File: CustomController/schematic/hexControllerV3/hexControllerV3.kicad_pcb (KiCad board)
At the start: 4 copper layers, 129 x 63.9 mm, 48 parts, among them IC1 ESP32-S2-MINI-1-N4R2, IC2 IP5306, J1 USB_C_Receptacle_USB2.0_16P, J2 Battery, J3 Switch1, J4 Switch2, J5 Switch3, J6 Switch4, J7 Battery, SW1 RotaryEncoder_Switch, SW2 SW_DIP_x01, SW3 SW_DIP_x01, SW4 SW_DIP_x01, SW5 SW_DIP_x01, SW6 SW_DIP_x01, U2 AMS1117-3.3

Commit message: Changed schematic/ PCB
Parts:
- moved J5 1.87 mm to (115.3, 59.8)
- moved J6 1.26 mm to (111.4, 59.8)
- moved J1 1.05 mm to (152.5, 53.8)
- moved SW6 0.60 mm to (149.4, 96.3)
- moved SW1 0.45 mm to (208.1, 74.5)
- moved SW2 0.45 mm to (100.9, 65.2)
- moved SW3 0.45 mm to (91.4, 74.7)
- moved SW4 0.45 mm to (100.9, 84.2)
- moved SW5 0.45 mm to (110.4, 74.7)
- moved VR1 0.35 mm to (125.1, 110.4)
- moved VR2 0.35 mm to (175.1, 110.4)
- moved LED5 0.32 mm to (152.6, 104.8)
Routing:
- net D-: track 15.5 -> 18.8 mm
- net GND: track 77.8 -> 81.0 mm
- net +5V USB: track 34.8 -> 37.9 mm
- net D+: track 16.4 -> 18.0 mm
- net Switch3: track 49.8 -> 50.9 mm
- net Net-(J1-CC2): track 10.4 -> 11.4 mm
- net Switch4: track 49.5 -> 50.1 mm
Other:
- outline, holes or cut-outs redrawn

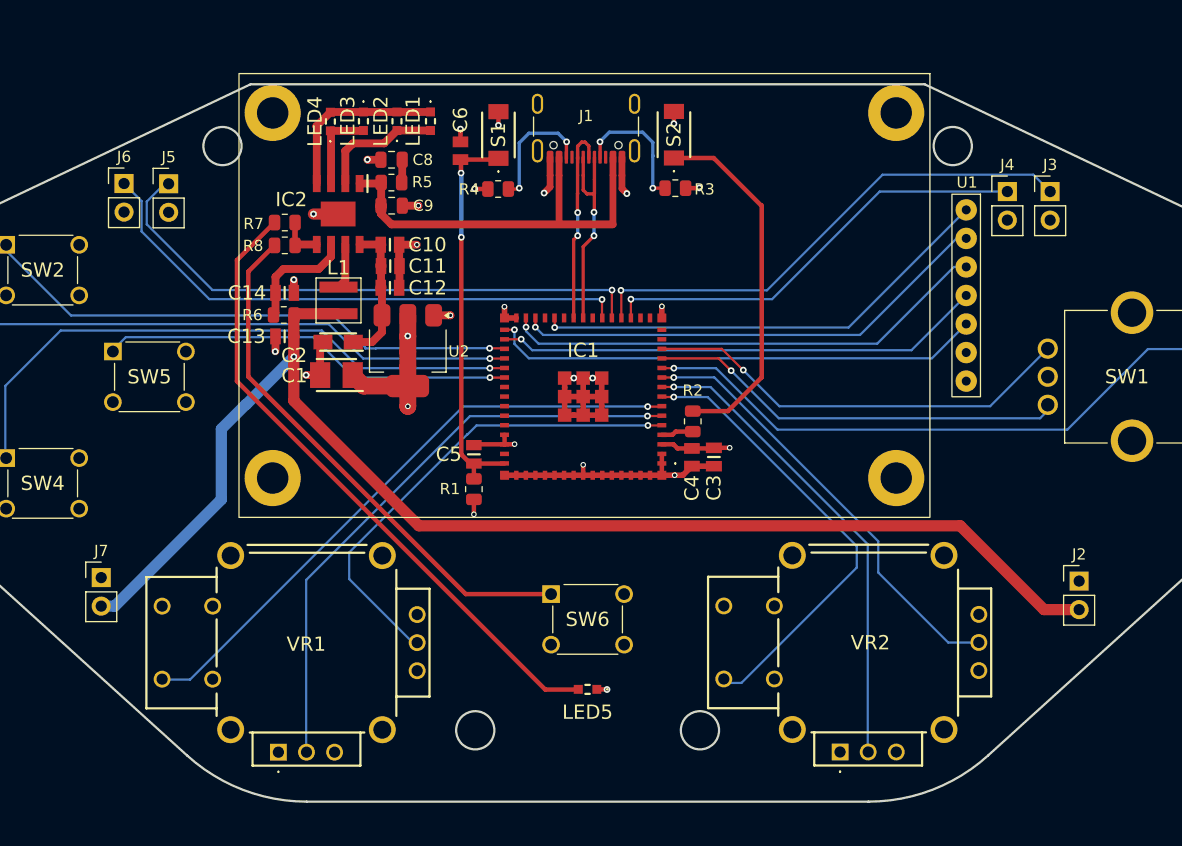
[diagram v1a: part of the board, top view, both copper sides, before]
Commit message: Altered controller schematic
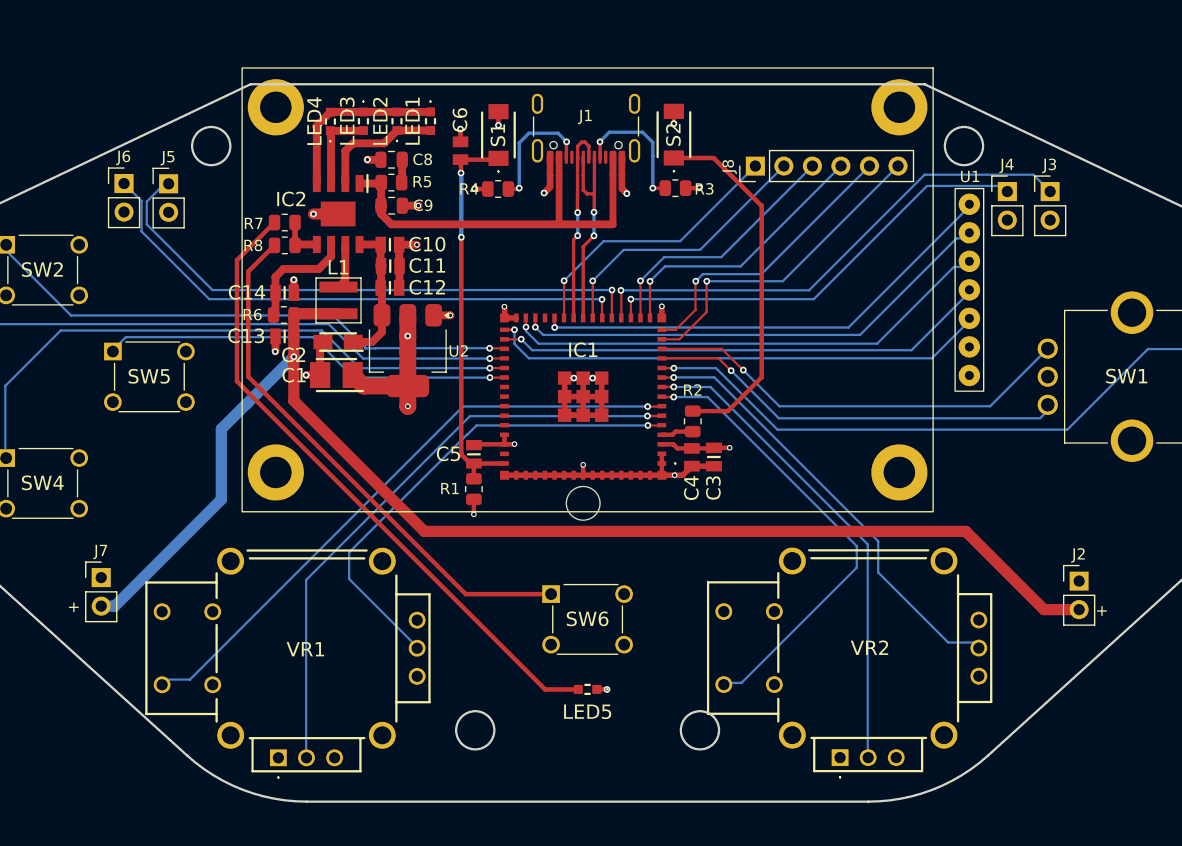
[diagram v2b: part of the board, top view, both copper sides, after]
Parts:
- added J8: Conn_01x06, Connector_PinHeader_2.54mm:PinHeader_1x06_P2.54mm_Vertical, F.Cu at (167.6, 58.2)
- moved U1 0.57 mm to (156.6, 69.2)
- moved VR1 0.50 mm to (125.1, 110.9)
- moved VR2 0.50 mm to (175.1, 110.9)
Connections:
- IC1 pad 14: unconnected-(IC1-IO10-Pad14) -> Spare1
- IC1 pad 15: unconnected-(IC1-IO11-Pad15) -> Spare2
- IC1 pad 16: unconnected-(IC1-IO12-Pad16) -> Spare3
- IC1 pad 17: unconnected-(IC1-IO13-Pad17) -> Spare4
- IC1 pad 22: unconnected-(IC1-IO18-Pad22) -> Spare5
- IC1 pad 25: unconnected-(IC1-IO21-Pad25) -> Spare6
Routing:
- net Spare1: track 0.00 -> 29.0 mm, vias 0 -> 1
- net Spare2: track 0.00 -> 26.0 mm, vias 0 -> 1
- net Spare6: track 0.00 -> 24.6 mm, vias 0 -> 1
- net Spare5: track 0.00 -> 24.5 mm, vias 0 -> 1
- net Spare3: track 0.00 -> 24.5 mm, vias 0 -> 1
- net Spare4: track 0.00 -> 22.9 mm, vias 0 -> 1
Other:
- outline, holes or cut-outs redrawn
- board text added: "+"

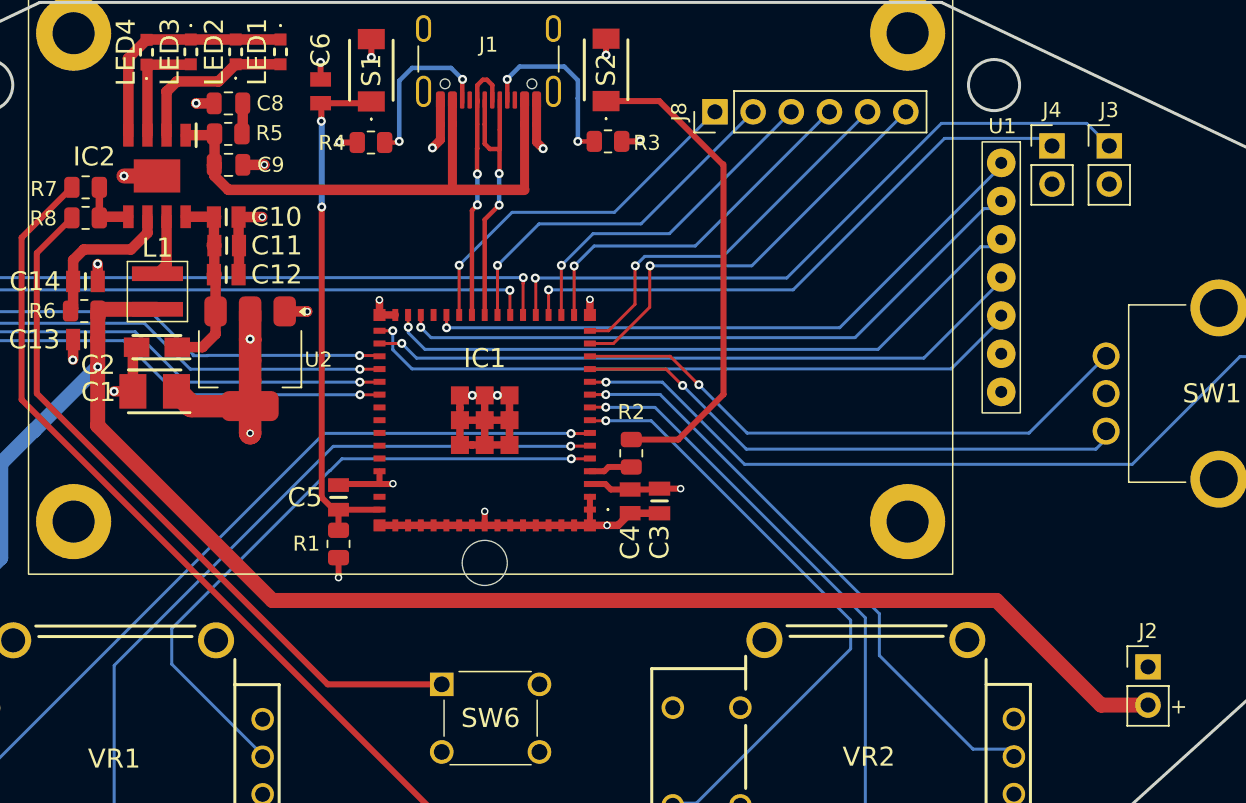
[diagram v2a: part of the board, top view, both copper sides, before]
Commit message: Corrected pin config for schematic
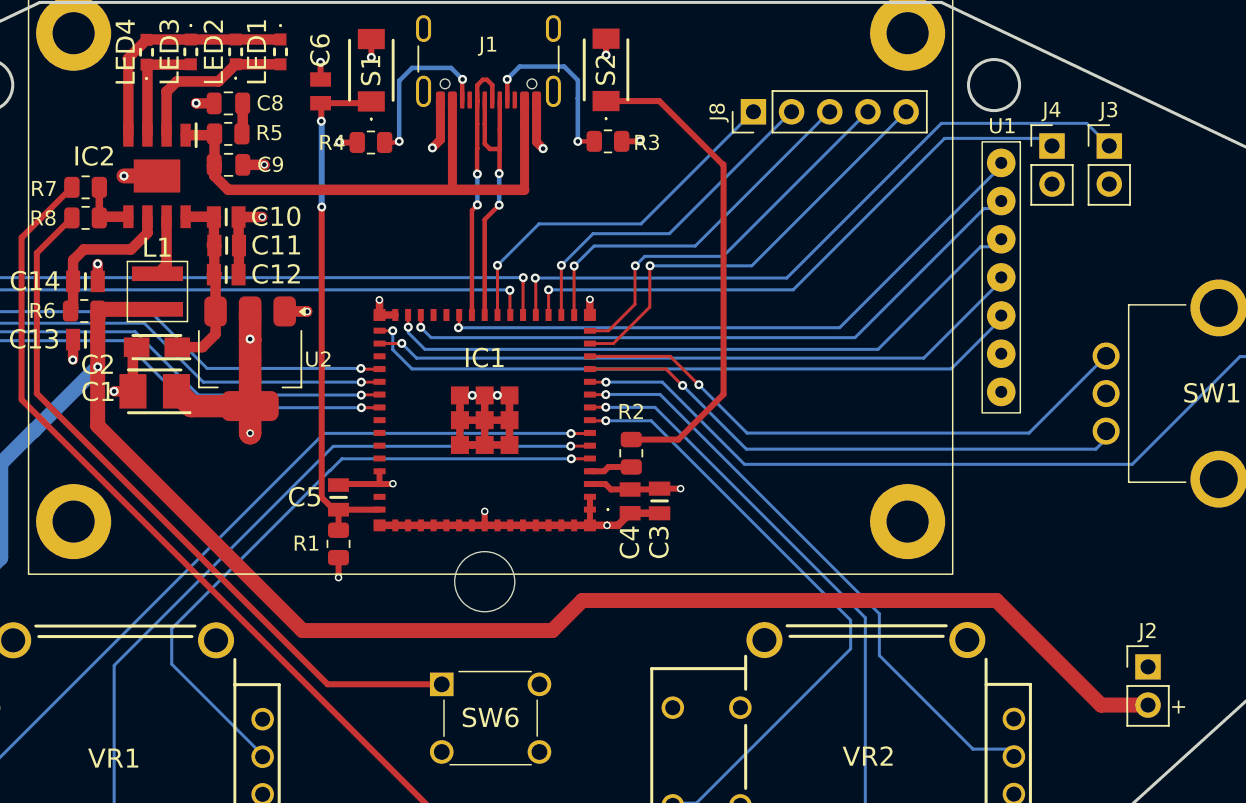
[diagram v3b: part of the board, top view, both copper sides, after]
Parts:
- J8: footprint Connector_PinHeader_2.54mm:PinHeader_1x06_P2.54mm_Vertical -> Connector_PinHeader_2.54mm:PinHeader_1x05_P2.54mm_Vertical
- moved J8 2.56 mm to (170.1, 58.2)
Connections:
- IC1 pad 25: Spare6 -> RST
- IC1 pad 26: RST -> unconnected-(IC1-IO26-Pad26)
- IC1 pad 33: button1 -> unconnected-(IC1-IO37-Pad33)
- IC1 pad 34: button2 -> button1
- IC1 pad 35: button3 -> button2
- IC1 pad 36: button4 -> button3
- IC1 pad 37: unconnected-(IC1-IO41-Pad37) -> button4
- J8 pad 1: Spare6 -> Spare5
- J8 pad 2: Spare5 -> Spare4
- J8 pad 3: Spare4 -> Spare3
- J8 pad 4: Spare3 -> Spare2
- J8 pad 5: Spare2 -> Spare1
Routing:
- net Spare6: track 24.6 -> 0.00 mm, vias 1 -> 0
- net Net-(J2-Pin_2): track 122.4 -> 124.1 mm
- net RST: track 41.8 -> 41.0 mm
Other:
- outline, holes or cut-outs redrawn

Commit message: Editted schematic
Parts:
- added C15: 100nF, Capacitor_SMD:C_0805_2012Metric_Pad1.18x1.45mm_HandSolder, F.Cu at (166.0, 65.2)
- added C16: 100nF, Capacitor_SMD:C_0805_2012Metric_Pad1.18x1.45mm_HandSolder, F.Cu at (158.9, 65.2)
- added C7: 100nF, Capacitor_SMD:C_0805_2012Metric_Pad1.18x1.45mm_HandSolder, F.Cu at (147.3, 89.9)
- added R10: 4.7K, Resistor_SMD:R_0805_2012Metric, F.Cu at (162.8, 71.1)
- added R9: 4.7K, Resistor_SMD:R_0805_2012Metric, F.Cu at (162.9, 73.1)
- added U3: INA260, Package_SO:TSSOP-16_4.4x5mm_P0.65mm, F.Cu at (152.4, 90.8)
- added U4: BMI330, SamacSys_Parts:BMI330, F.Cu at (162.4, 65.5)
- J8: footprint Connector_PinHeader_2.54mm:PinHeader_1x05_P2.54mm_Vertical -> Connector_PinHeader_2.54mm:PinHeader_2x04_P2.54mm_Vertical
- S1, S2: value TS-1088-AR02016 -> KMR731NG; footprint SamacSys_Parts:TS1088AR02016 -> Button_Switch_SMD:SW_Push_1P1T_NO_CK_KMR2
- moved J8 6.19 mm to (174.6, 54.0), turned to -90 degrees
- moved J1 0.50 mm to (152.5, 53.3)
- turned S2 to -90 degrees
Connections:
- C13 pad 1: Net-(J2-Pin_2) -> INA260_OUT
- IC1 pad 14: Spare1 -> SDA
- IC1 pad 15: Spare2 -> SCL
- IC1 pad 16: Spare3 -> BMI330_INT1
- IC1 pad 17: Spare4 -> BMI330_INT2
- IC1 pad 22: Spare5 -> INA260_INT
- IC1 pad 26: unconnected-(IC1-IO26-Pad26) -> GPIO26
- IC1 pad 33: unconnected-(IC1-IO37-Pad33) -> GPIO37
- IC1 pad 38: unconnected-(IC1-IO42-Pad38) -> GPIO42
- IC1 pad 39: unconnected-(IC1-TXD0-Pad39) -> TX
- IC1 pad 40: unconnected-(IC1-RXD0-Pad40) -> RX
- J8 pad 1: Spare5 -> +5V
- J8 pad 2: Spare4 -> +3V3
- J8 pad 3: Spare3 -> RX
- J8 pad 4: Spare2 -> TX
- J8 pad 5: Spare1 -> GPIO42
- L1 pad 2: Net-(J2-Pin_2) -> INA260_OUT
- R6 pad 1: Net-(J2-Pin_2) -> INA260_OUT
- SW2 pad 2: GND -> unconnected-(SW2-Pad2)
- SW2 pad 3: (no net) -> GND
- SW2 pad 4: (no net) -> GND
- SW3 pad 2: GND -> unconnected-(SW3-Pad2)
- SW3 pad 3: (no net) -> GND
- SW3 pad 4: (no net) -> GND
- SW4 pad 2: GND -> unconnected-(SW4-Pad2)
- SW4 pad 3: (no net) -> GND
- SW4 pad 4: (no net) -> GND
- SW5 pad 2: GND -> unconnected-(SW5-Pad2)
- SW5 pad 3: (no net) -> GND
- SW5 pad 4: (no net) -> GND
- SW6 pad 2: GND -> unconnected-(SW6-Pad2)
- SW6 pad 3: (no net) -> GND
- SW6 pad 4: (no net) -> GND
- U1 pad 7: +3V3 -> +5V
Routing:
- net +5V: track 13.1 -> 89.4 mm, vias 0 -> 1
- net RX: track 0.00 -> 48.7 mm, vias 0 -> 1
- net TX: track 0.00 -> 44.3 mm, vias 0 -> 1
- net GPIO42: track 0.00 -> 44.2 mm, vias 0 -> 1
- net INA260_OUT: track 0.00 -> 42.6 mm
- net GPIO37: track 0.00 -> 39.6 mm, vias 0 -> 1
- net GPIO26: track 0.00 -> 32.1 mm, vias 0 -> 1
- net SCL: track 0.00 -> 31.1 mm, vias 0 -> 2
- net Spare1: track 29.0 -> 0.00 mm, vias 1 -> 0
- net SDA: track 0.00 -> 27.8 mm, vias 0 -> 2
- net Spare2: track 26.0 -> 0.00 mm, vias 1 -> 0
- net Spare5: track 24.5 -> 0.00 mm, vias 1 -> 0
- net Spare3: track 24.5 -> 0.00 mm, vias 1 -> 0
- net Spare4: track 22.9 -> 0.00 mm, vias 1 -> 0
- net INA260_INT: track 0.00 -> 20.1 mm, vias 0 -> 2
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- added copper zone on F.Cu, net +3V3
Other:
- outline, holes or cut-outs redrawn
- board text added: "26"
- board text added: "37"
- board text added: "3V3"
- board text added: "42"
- board text added: "5V"
- board text added: "BOOT"
- board text added: "GND"
- board text added: "RESET"
- board text added: "RX"
- board text added: "TX"

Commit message: Updated controller schematic
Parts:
- removed C10, C11, C12, C13, C14: 22uF, SamacSys_Parts:CAPC2012X140N
- removed C2: 10uF, SamacSys_Parts:CAPPM3216X180N
- removed C8, C9: 10uF, Capacitor_SMD:C_0805_2012Metric
- removed IC2: IP5306, SamacSys_Parts:SOIC127P600X165-9N
- removed L1: 1uH, SamacSys_Parts:XAL40XX
- removed LED1, LED2, LED3, LED4, LED5: ~, SamacSys_Parts:KP1608SURCK
- removed R7: 20R, Resistor_SMD:R_0805_2012Metric
- removed R8: 10k, Resistor_SMD:R_0805_2012Metric
- removed SW6: SW_DIP_x01, SamacSys_Parts:DTS62NV
- added C17: 10uF, Capacitor_SMD:C_0603_1608Metric_Pad1.08x0.95mm_HandSolder, F.Cu at (125.2, 61.4)
- added C18: 10uF, Capacitor_SMD:C_0603_1608Metric_Pad1.08x0.95mm_HandSolder, F.Cu at (126.8, 61.4)
- added C19: 100nF, Capacitor_SMD:C_0603_1608Metric_Pad1.08x0.95mm_HandSolder, F.Cu at (133.2, 66.3)
- added C20: 22uF, Capacitor_SMD:C_0603_1608Metric_Pad1.08x0.95mm_HandSolder, F.Cu at (137.8, 61.4)
- added C21: 22uF, Capacitor_SMD:C_0603_1608Metric_Pad1.08x0.95mm_HandSolder, F.Cu at (136.3, 61.4)
- added C22: 22uF, Capacitor_SMD:C_0603_1608Metric_Pad1.08x0.95mm_HandSolder, F.Cu at (134.8, 61.3)
- added IC3: TPS63020DSJR, SamacSys_Parts:TPS63020DSJR, F.Cu at (130.8, 62.4)
- added L2: 1.5uH, SamacSys_Parts:XAL40XX, F.Cu at (130.8, 56.6)
- added Q1: DMG9926UDM, Package_TO_SOT_SMD:SOT-23-6, F.Cu at (131.0, 83.6)
- added R11: 1M, Resistor_SMD:R_0603_1608Metric, F.Cu at (137.9, 64.5)
- added R12: 180K, Resistor_SMD:R_0603_1608Metric, F.Cu at (135.7, 65.3)
- C1: value 22uF -> 100nF; footprint SamacSys_Parts:CAPPM3528X210N -> SamacSys_Parts:CAPC2012X95N
- R5: value 2R -> 1k
- R6: value 0.5R -> 100R
- U2: value AMS1117-3.3 -> DW01A; footprint Package_TO_SOT_SMD:SOT-223-3_TabPin2 -> Package_TO_SOT_SMD:SOT-23-6
- moved R5 21.7 mm to (127.2, 79.9)
- moved R6 12.4 mm to (134.7, 80.0), turned to 0 degrees
- moved U2 7.72 mm to (130.9, 79.9), turned to 0 degrees
- moved C1 6.61 mm to (134.7, 81.8)
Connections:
- C1 pad 1: +3V3 -> Net-(J2-Pin_1)
- C1 pad 2: GND -> Net-(U2-VCC)
- J2 pad 1: GND -> Net-(J2-Pin_1)
- J2 pad 2: Net-(J2-Pin_2) -> BAT+
- J7 pad 1: GND -> Net-(J2-Pin_1)
- J7 pad 2: Net-(J2-Pin_2) -> BAT+
- R5 pad 1: +5V USB -> GND
- R5 pad 2: Net-(C8-Pad1) -> Net-(U2-CS)
- R6 pad 1: INA260_OUT -> Net-(U2-VCC)
- R6 pad 2: Net-(IC2-BAT) -> BAT+
- U2 pad 1: GND -> Net-(Q1-G2)
- U2 pad 2: +3V3 -> Net-(U2-CS)
- U2 pad 3: +5V -> Net-(Q1-G1)
- U3 pad 1: Net-(J2-Pin_2) -> BAT+
- U3 pad 12: Net-(J2-Pin_2) -> BAT+
- U3 pad 2: Net-(J2-Pin_2) -> BAT+
- U3 pad 3: Net-(J2-Pin_2) -> BAT+
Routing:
- net Net-(J2-Pin_2): track 125.8 -> 0.00 mm
- net BAT+: track 0.00 -> 125.8 mm
- net Net-(LED5-A): track 56.9 -> 0.00 mm, vias 2 -> 0
- net Net-(R8-Pad2): track 47.6 -> 0.00 mm, vias 2 -> 0
- net INA260_OUT: track 42.6 -> 8.80 mm
- net +5V USB: track 38.9 -> 13.0 mm
- net Net-(IC3-EN): track 0.00 -> 19.7 mm
- net Net-(IC2-LED3): track 15.8 -> 0.00 mm
- net +5V: track 89.4 -> 76.6 mm, vias 1 -> 0
- net GND: track 99.4 -> 86.8 mm, vias 28 -> 41
- net Net-(IC2-LED1): track 11.3 -> 0.00 mm
- net Net-(IC2-BAT): track 10.2 -> 0.00 mm
- net Net-(J2-Pin_1): track 0.00 -> 9.43 mm
- net Net-(IC2-LED2): track 8.09 -> 0.00 mm
- net Net-(Q1-G2): track 0.00 -> 7.73 mm
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- added copper zone on F.Cu, net +5V
- added copper zone on F.Cu, net GND
